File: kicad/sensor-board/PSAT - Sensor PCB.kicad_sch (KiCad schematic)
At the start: 56 parts, among them J1 533980471, J2 533980471, J3 533980471, J4 533980471, Q1 2N2222A, U1 ESP32-CAM, U2 CD-PA1616D, U3 BME280, U4 BMI323, U5 ADXL375, U6 ADXL345

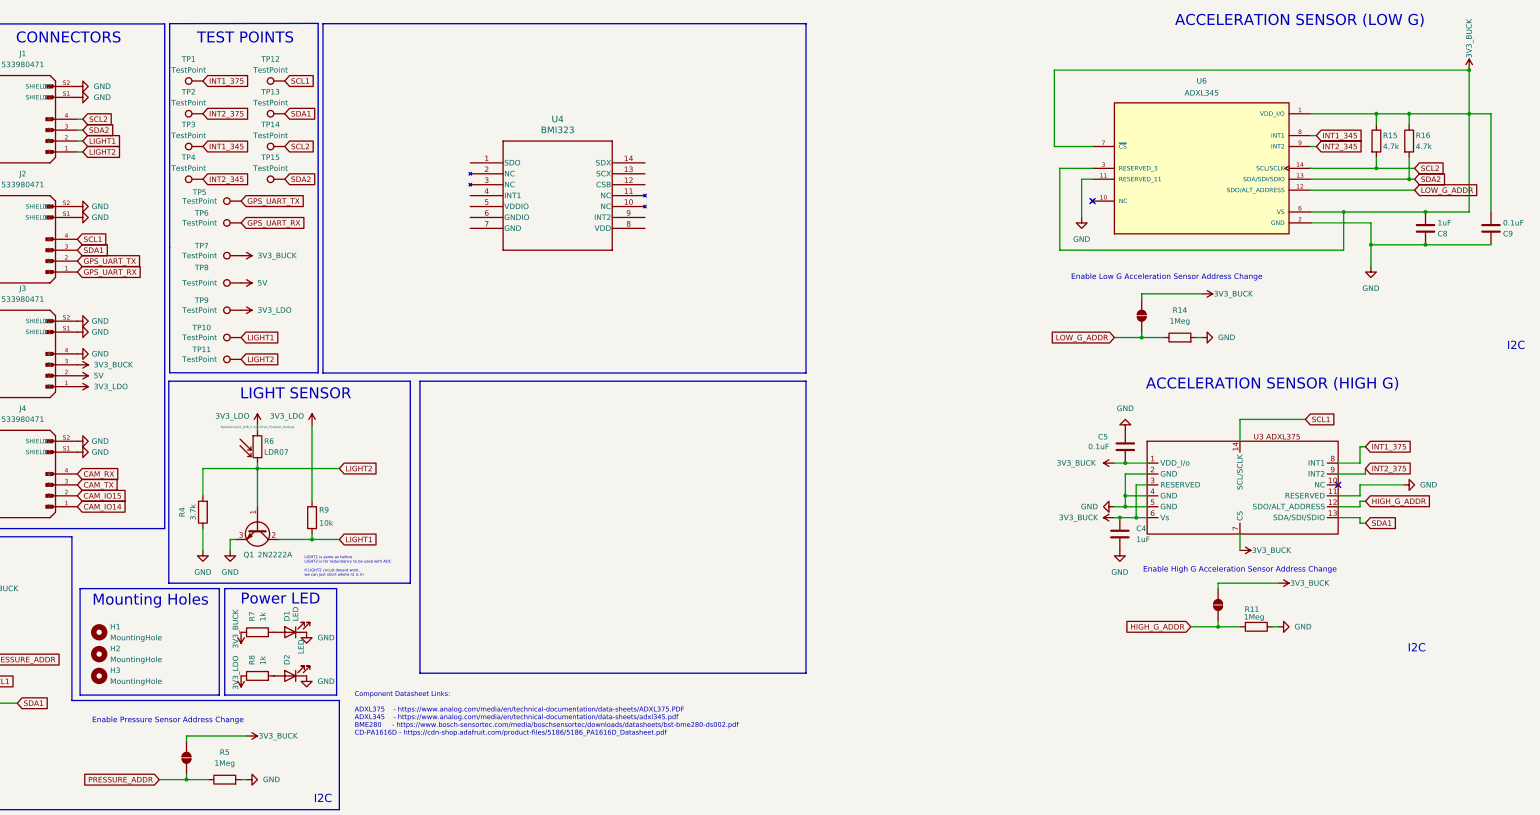
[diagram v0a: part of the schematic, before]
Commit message: feat: Wiring sensor board, incomplete
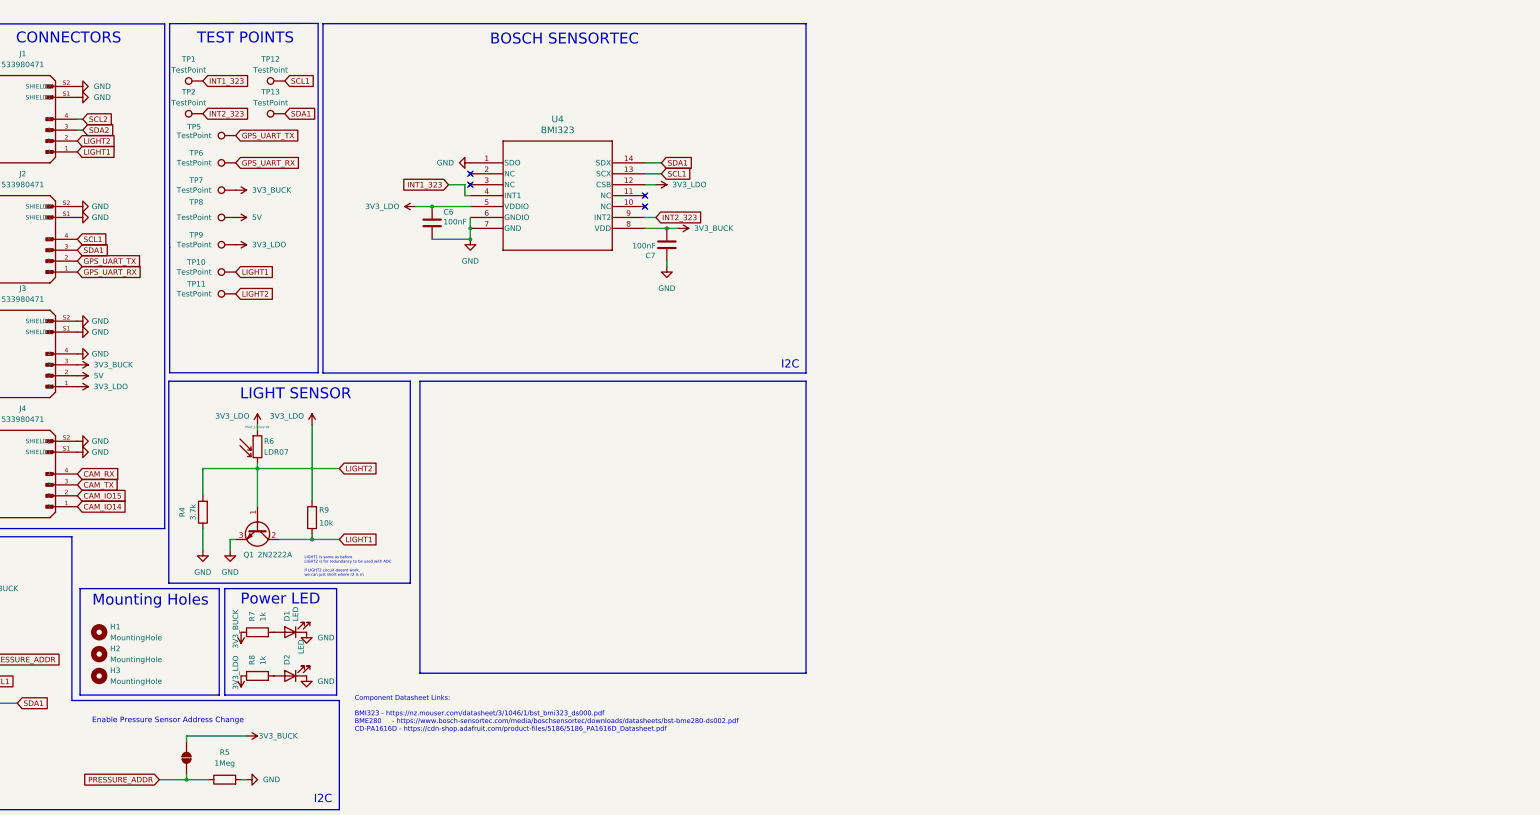
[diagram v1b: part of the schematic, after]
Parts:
- removed C4, C8: 1uF, Capacitor_SMD:C_0805_2012Metric_Pad1.18x1.45mm_HandSolder, symbol Device:C
- removed C5, C9: 0.1uF, Capacitor_SMD:C_0805_2012Metric_Pad1.18x1.45mm_HandSolder, symbol Device:C
- removed JP5, JP6: EN_5, Jumper:SolderJumper-2_P1.3mm_Open_Pad1.0x1.5mm, symbol Jumper:SolderJumper_2_Open
- removed R11, R14: 1Meg, Resistor_SMD:R_0805_2012Metric_Pad1.20x1.40mm_HandSolder, symbol Device:R
- removed R15, R16: 4.7k, Resistor_SMD:R_0805_2012Metric_Pad1.20x1.40mm_HandSolder, symbol Device:R
- removed TP14, TP15, TP3, TP4: TestPoint, TestPoint:TestPoint_Pad_D1.0mm, symbol Connector:TestPoint
- removed U5: ADXL375, ADXL375:adxl375, symbol New_Library:ADXL375
- removed U6: ADXL345, ADXL345:adxl345, symbol adxl345:ADXL345
- added C6, C7: 100nF, Capacitor_SMD:C_0805_2012Metric_Pad1.18x1.45mm_HandSolder, symbol Device:C
- R6: footprint OptoDevice:R_LDR_5.1x4.3mm_P3.4mm_Vertical -> PSAT_Library:ldr
- U4: footprint BMI323:BMI323_BOS -> BMI323:BMI323_BOS-M
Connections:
- net INT1_375 is gone; now on net INT1_323: TP1.1
- net INT2_375 is gone; now on net INT2_323: TP2.1
- net 3V3_BUCK: now also U4.8 (VDD), C7.1
- net 3V3_LDO: now also U4.12 (CSB), U4.5 (VDDIO), C6.2
- net GND: now also U4.1 (SDO), U4.6 (GNDIO), U4.7 (GND), C6.1, C7.2
- net LIGHT1: now also J1.1; no longer J1.2
- net LIGHT2: now also J1.2; no longer J1.1
- net SCL1: now also U4.13 (SCX)
- net SDA1: now also U4.14 (SDX)
- net INT1_323: now reaches U4.4 (INT1)
- net INT2_323: now reaches U4.9 (INT2)
- no-connect marks 18 -> 20
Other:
- note added: "BOSCH SENSORTEC"
- note added: "Component Datasheet Links: BMI323 - https://nz.mouser.com/datasheet/3/1046/1/bst_bmi323_ds000.pdf BME280 - https://www.bosch-sensortec.com/media/boschsensortec/downloads/datasheets/bst-bme280-ds002.pdf CD-PA1616D - https://cdn-shop.adafruit.com/product-files/5186/5186_PA1616D_Datasheet.pdf"
- note removed: "ACCELERATION SENSOR (HIGH G)"
- note removed: "ACCELERATION SENSOR (LOW G)"
- note removed: "Component Datasheet Links: ADXL375 - https://www.analog.com/media/en/technical-documentation/data-sheets/ADXL375.PDF ADXL345 - https://www.analog.com/media/en/technical-documentation/data-sheets/adxl345.pdf BME280 - https://www.bosch-sensortec.com/media/boschsensortec/downloads/datasheets/bst-bme280-ds002.pdf CD-PA1616D - https://cdn-shop.adafruit.com/product-files/5186/5186_PA1616D_Datasheet.pdf"
- note removed: "Enable High G Acceleration Sensor Address Change"
- note removed: "Enable Low G Acceleration Sensor Address Change"
- moved on the sheet: TP10, TP11, TP5, TP6, TP7, TP8, TP9

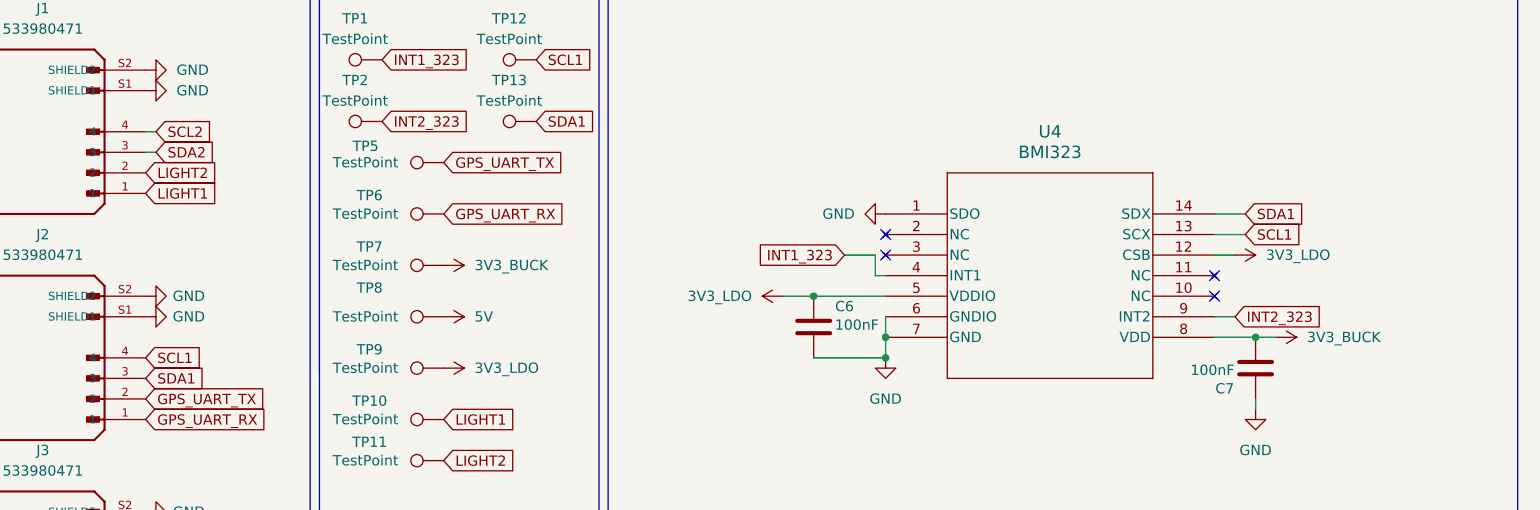
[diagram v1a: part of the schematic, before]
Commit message: feat: wiring sensor board
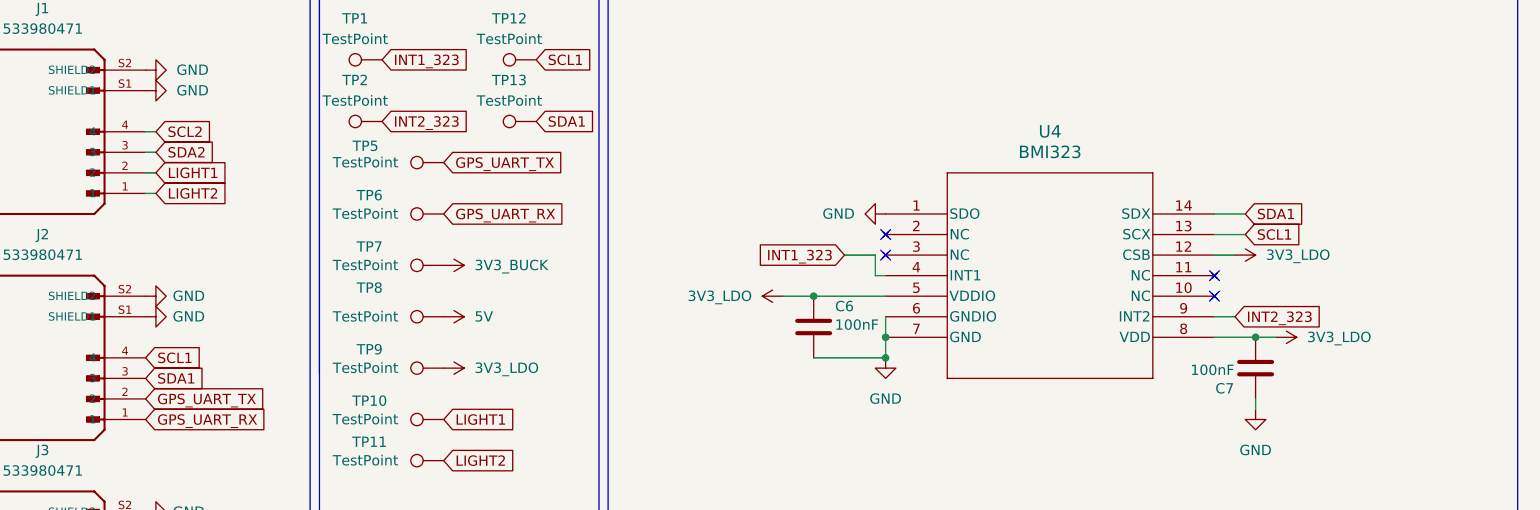
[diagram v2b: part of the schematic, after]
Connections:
- net 3V3_BUCK: no longer C7.1, U4.8 (VDD)
- net 3V3_LDO: now also C7.1, U4.8 (VDD)
- net LIGHT1: now also J1.2; no longer J1.1
- net LIGHT2: now also J1.1; no longer J1.2
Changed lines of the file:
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@@
 	(wire
 		(pts
+			(xy 115.57 40.64) (xy 114.3 40.64)
+		)
+		(stroke
+			(width 0)
+			(type default)
+		)
+	)
+	(wire
+		(pts
 			(xy 53.34 184.15) (xy 53.34 187.96)
 		)
@@
 	(wire
 		(pts
+			(xy 115.57 43.18) (xy 114.3 43.18)
+		)
+		(stroke
+			(width 0)
+			(type default)
+		)
+	)
+	(wire
+		(pts
 			(xy 196.85 55.88) (xy 205.74 55.88)
 		)
@@
 	(global_label "LIGHT1"
 		(shape input)
-		(at 114.3 43.18 0)
+		(at 115.57 40.64 0)
 		(fields_autoplaced yes)
 		(effects
@@
 		)
 		(property "Intersheetrefs" "${INTERSHEET_REFS}"
-			(at 123.6957 43.18 0)
+			(at 124.9657 40.64 0)
 			(effects
 				(font
@@
 	(global_label "LIGHT2"
 		(shape input)
-		(at 114.3 40.64 0)
+		(at 115.57 43.18 0)
 		(fields_autoplaced yes)
 		(effects
@@
 		)
 		(property "Intersheetrefs" "${INTERSHEET_REFS}"
-			(at 123.6957 40.64 0)
+			(at 124.9657 43.18 0)
 			(effects
 				(font
@@
 			)
 		)
-		(property "Value" "3V3_BUCK"
+		(property "Value" "3V3_LDO"
 			(at 257.81 60.9599 90)
 			(effects

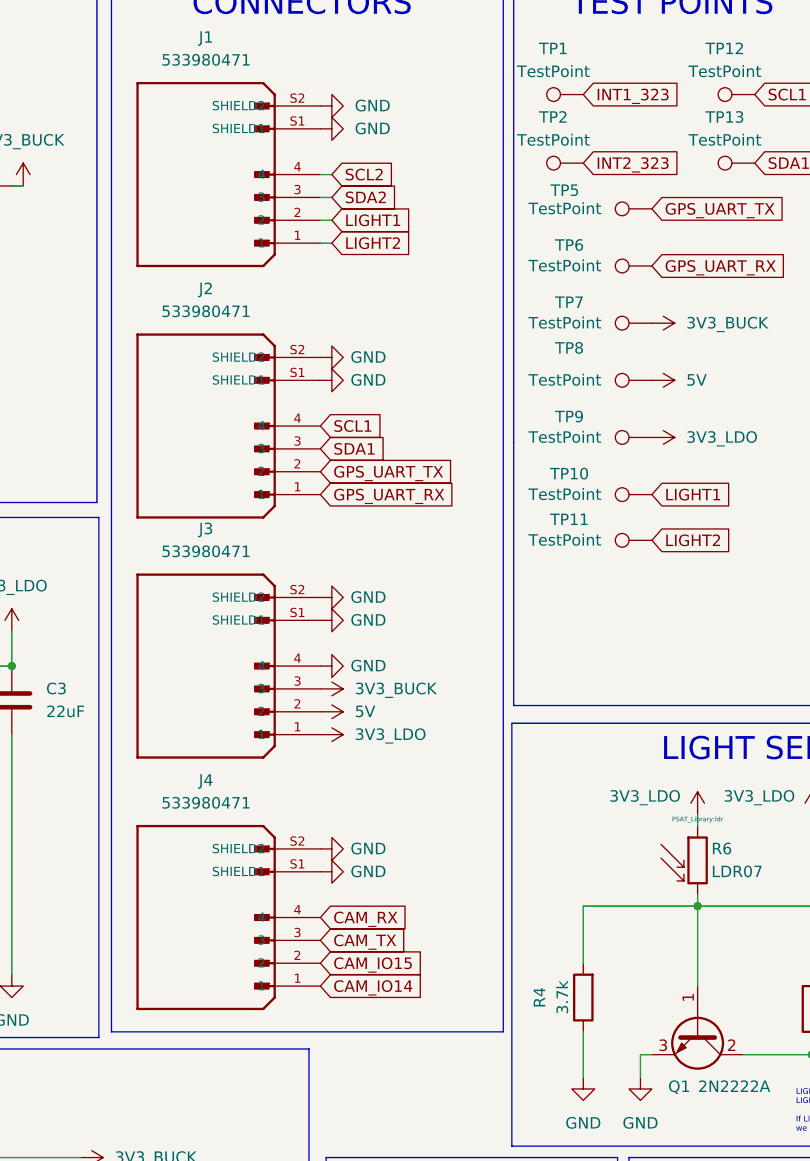
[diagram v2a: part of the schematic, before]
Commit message: feat: added high g accel foot/sym
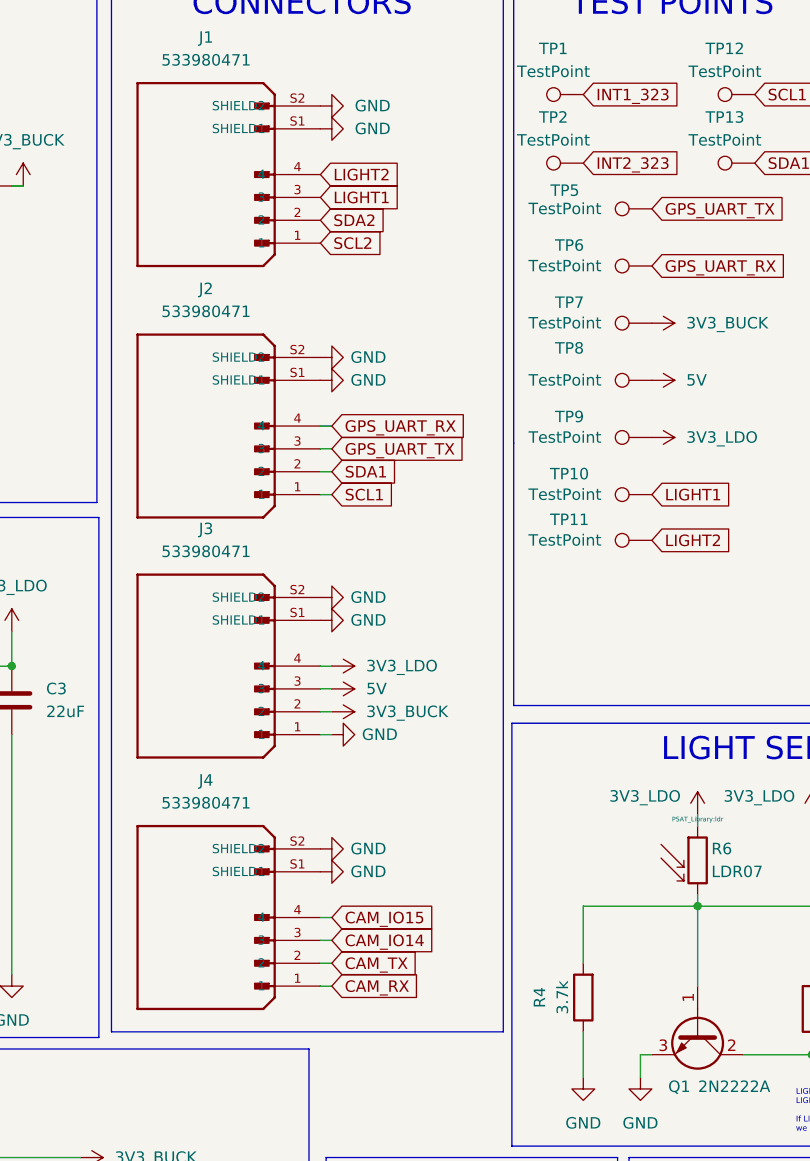
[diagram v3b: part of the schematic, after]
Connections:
- net 3V3_BUCK: now also J3.2; no longer J3.3
- net 3V3_LDO: now also J3.4; no longer J3.1
- net 5V: now also J3.3; no longer J3.2
- net CAM_IO14: now also J4.3; no longer J4.1
- net CAM_IO15: now also J4.4; no longer J4.2
- net CAM_RX: now also J4.1; no longer J4.4
- net CAM_TX: now also J4.2; no longer J4.3
- net GND: now also J3.1; no longer J3.4
- net GPS_UART_RX: now also J2.4; no longer J2.1
- net GPS_UART_TX: now also J2.3; no longer J2.2
- net LIGHT1: now also J1.3; no longer J1.2
- net LIGHT2: now also J1.4; no longer J1.1
- net SCL1: now also J2.1; no longer J2.4
- net SCL2: now also J1.1; no longer J1.4
- net SDA1: now also J2.2; no longer J2.3
- net SDA2: now also J1.2; no longer J1.3
